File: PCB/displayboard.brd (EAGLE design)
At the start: 100 x 80 mm, 9 parts

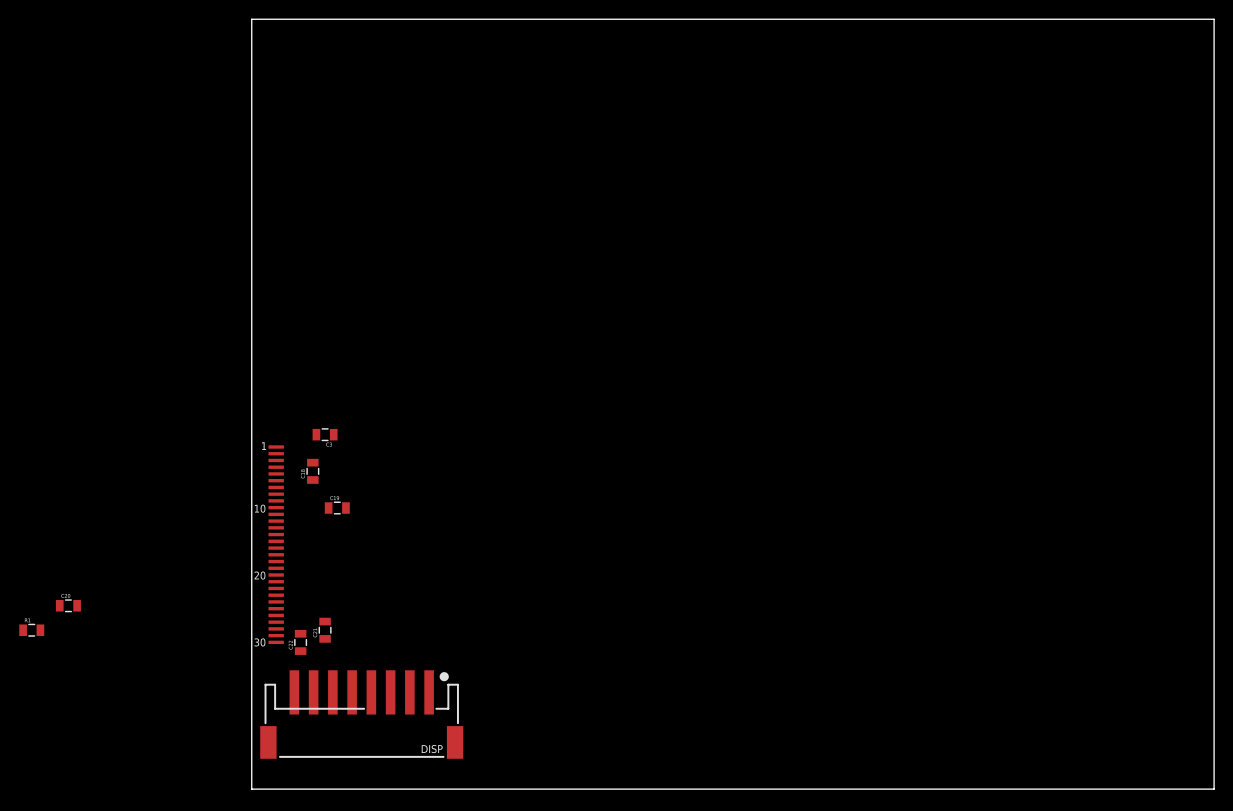
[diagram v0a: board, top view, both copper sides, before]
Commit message: Displayboard completed.. Need to check connector width
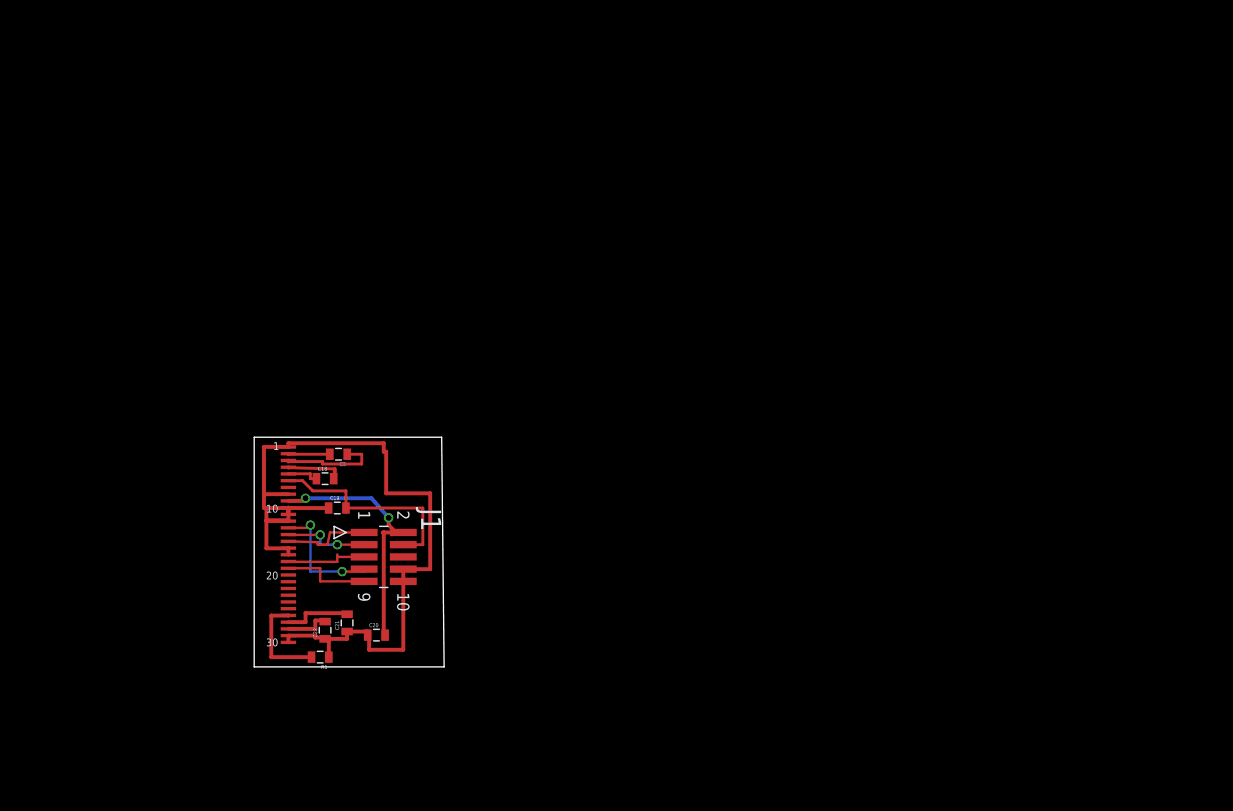
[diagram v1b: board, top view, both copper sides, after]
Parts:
- removed DISP: (no value), microbuilder:JSTPH8
- added J1: FTSH-105-01-L-DV, SAMTEC-HTSW-FTxx_By_element14_Batch_1:SAMTEC_FTSH-105-01-L-DV
- C19, C20: value (none) -> 2.2u
- C21: value 2.2uF -> 4.7uF
- moved C20 32.1 mm to (13.0, 16.0)
- moved R1 30.1 mm to (7.11, 13.7), turned to 180 degrees
- moved C22 2.84 mm to (7.62, 16.5)
- moved C3 2.47 mm to (9.02, 34.8)
- moved C21 2.41 mm to (9.91, 17.3)
- moved C18 1.48 mm to (7.62, 32.3), turned to 0 degrees
- moved U$1 1.27 mm to (3.81, 25.4)
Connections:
- net 3.3V: now also J1.2; no longer DISP.2
- net DISP_CS: now also J1.7; no longer DISP.5
- net DISP_DC: now also J1.1; no longer DISP.7
- net GND: now also J1.10, J1.8, U$1.16, U$1.17; no longer DISP.8
- net RST: now also J1.3; no longer DISP.3
- net SPI0_MOSI: now also J1.9; no longer DISP.6
- net SPI0_SCK: now also J1.5; no longer DISP.4
- net VBAT: now also J1.4; no longer DISP.1
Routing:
- net GND: track 0.00 -> 89.3 mm
- net 3.3V: track 0.00 -> 26.2 mm, vias 0 -> 2
- net VBAT: track 0.00 -> 22.0 mm
- net DISP_CS: track 0.00 -> 13.2 mm, vias 0 -> 2
- net N$27: track 0.00 -> 10.5 mm
- net N$3: track 0.00 -> 10.3 mm
- net SPI0_MOSI: track 0.00 -> 9.23 mm
- net DISP_DC: track 0.00 -> 9.17 mm
- net RST: track 0.00 -> 8.92 mm, vias 0 -> 2
- net SPI0_SCK: track 0.00 -> 8.66 mm
- net N$28: track 0.00 -> 7.15 mm
- net N$29: track 0.00 -> 5.92 mm
- net N$26: track 0.00 -> 4.80 mm
- net N$25: track 0.00 -> 4.36 mm
- net N$2: track 0.00 -> 3.43 mm
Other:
- board size 100 x 80 mm -> 19.7 x 23.9 mm

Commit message: Final version of both PCBs.. Send to OSHPark
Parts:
- removed C18: (no value), SparkFun-Capacitors:0805
- removed C19, C20: 2.2u, SparkFun-Capacitors:0805
- removed C21: 4.7uF, SparkFun-Capacitors:0805
- removed C22: 10uF, SparkFun-Capacitors:0805
- added C1, C2: 1uF, SparkFun-Capacitors:0805
- added C4: 2.2u, SparkFun-Capacitors:0805
- added C5: 4.7uF, SparkFun-Capacitors:0805
- added C6: 10uF, SparkFun-Capacitors:0805
- added DISP_SW: (no value), SparkFun-Electromechanical:KSA_SEALED_TAC_SWITCH
- C3: value (none) -> 2.2u
- U$1: device adafruit:1X30-0.7MM -> adafruit:1X28-0.32MM
- moved C3 27.9 mm to (9.27, 6.86), turned to 270 degrees
- moved U$1 24.7 mm to (4.95, 0.76), turned to 90 degrees
- moved J1 7.88 mm to (5.84, 24.0), turned to 0 degrees
- moved R1 1.80 mm to (8.38, 12.4)
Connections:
- new net DISP_SW: DISP_SW.P$1, J1.8
- net 3.3V: now also C4.2, U$1.P$8; no longer C20.2, U$1.9
- net DISP_CS: now also U$1.P$11; no longer U$1.13
- net DISP_DC: now also U$1.P$13; no longer U$1.15
- net GND: now also C3.1, C4.1, C5.1, C6.1, DISP_SW.P$3, U$1.P$1, U$1.P$10, U$1.P$27, U$1.P$28, U$1.P$7, U$1.P$9; no longer C19.1, C20.1, C21.1, C22.1, J1.8, U$1.1, U$1.10, U$1.11, U$1.12, U$1.16, U$1.17, U$1.29, U$1.30, U$1.8
- net N$2: now also C2.1, U$1.P$5; no longer C18.1, U$1.5
- net N$25: now also C1.2, U$1.P$2; no longer C3.2, U$1.2
- net N$26: now also C6.2, U$1.P$26; no longer C22.2, U$1.28
- net N$27: now also C1.1, U$1.P$3; no longer C3.1, U$1.3
- net N$28: now also C5.2, U$1.P$25; no longer C21.2, U$1.27
- net N$29: now also C2.2, U$1.P$4; no longer C18.2, U$1.4
- net N$3: now also U$1.P$24; no longer U$1.26
- net RST: now also U$1.P$12; no longer U$1.14
- net SPI0_MOSI: now also U$1.P$17; no longer U$1.19
- net SPI0_SCK: now also U$1.P$16; no longer U$1.18
- net VBAT: now also C3.2, U$1.P$6; no longer C19.2, U$1.6
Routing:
- net GND: track 89.3 -> 51.5 mm, vias 0 -> 3
- net VBAT: track 22.0 -> 39.2 mm
- net DISP_SW: track 0.00 -> 16.0 mm
- net DISP_DC: track 9.17 -> 22.4 mm, vias 0 -> 2
- net DISP_CS: track 13.2 -> 26.1 mm, vias 2 -> 0
- net RST: track 8.92 -> 16.5 mm, vias 2 -> 0
- net SPI0_MOSI: track 9.23 -> 14.9 mm, vias 0 -> 2
- net N$27: track 10.5 -> 4.92 mm
- net N$3: track 10.3 -> 4.84 mm
- net SPI0_SCK: track 8.66 -> 13.8 mm
- net N$29: track 5.92 -> 2.39 mm
- net 3.3V: track 26.2 -> 28.6 mm, vias 2 -> 0
- net N$26: track 4.80 -> 2.79 mm
- net N$25: track 4.36 -> 2.38 mm
- net N$28: track 7.15 -> 5.19 mm
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- added copper zone on layer 1, net GND
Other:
- board size 19.7 x 23.9 mm -> 17.4 x 29.5 mm
- board text added: "SwiMate Display Board 1.0 P. Bartell Spring 2014"
